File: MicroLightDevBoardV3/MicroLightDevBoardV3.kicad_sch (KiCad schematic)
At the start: 26 parts, among them J1 TYPE-C-31-M-12, J2 Conn_01x02_Socket, J3 Conn_01x03_Socket, SW1 SW_Push, U1 USBLC6-2P6, U2 STM32C071GBUx, U3 BQ25180, U4 S-85S1AB33-I6T1U

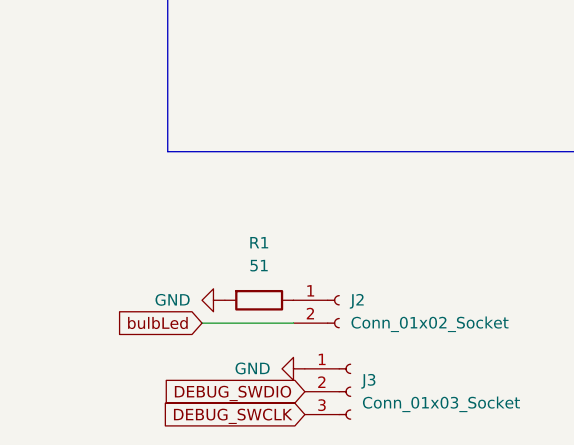
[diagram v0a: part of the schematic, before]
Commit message: adjusted debug pins to have smaller solder mask in vertical direction, changed bulb pins to both be circles and deleted 3d model, add usb 3d model
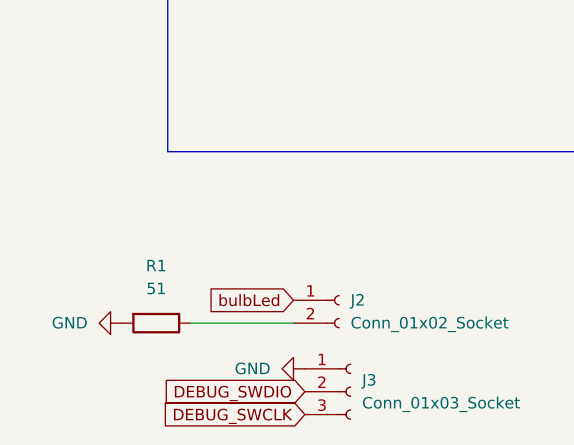
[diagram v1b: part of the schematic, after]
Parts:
- J3: footprint Connector_PinSocket_2.54mm:PinSocket_1x03_P2.54mm_Vertical -> MicroLightDevBoard:PinSocket_1x03_P2.54mm_Vertical_debug
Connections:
- net bulbLed: now also J2.1 (Pin_1); no longer J2.2 (Pin_2)
- net at R1.1: now also J2.2 (Pin_2); no longer J2.1 (Pin_1)
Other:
- moved on the sheet: R1
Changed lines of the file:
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@@
 	)
 	(no_connect
-		(at 19.05 63.5)
+		(at 41.91 55.88)
 	)
 	(no_connect
-		(at 41.91 55.88)
+		(at 19.05 63.5)
 	)
 	(no_connect
@@
 	(wire
 		(pts
-			(xy 36.83 177.8) (xy 46.99 177.8)
+			(xy 93.98 26.67) (xy 92.71 26.67)
 		)
 		(stroke
@@
 	(wire
 		(pts
-			(xy 93.98 26.67) (xy 92.71 26.67)
+			(xy 227.33 66.04) (xy 227.33 60.96)
 		)
 		(stroke
@@
 	(wire
 		(pts
-			(xy 227.33 66.04) (xy 227.33 60.96)
+			(xy 35.56 177.8) (xy 46.99 177.8)
 		)
 		(stroke
@@
 		)
 	)
-	(global_label "bulbLed"
-		(shape input)
-		(at 36.83 177.8 180)
-		(fields_autoplaced yes)
-		(effects
-			(font
-				(size 1.27 1.27)
-			)
-			(justify right)
-		)
-		(property "Intersheetrefs" "${INTERSHEET_REFS}"
-			(at 26.4669 177.8 0)
-			(effects
-				(font
-					(size 1.27 1.27)
-				)
-				(justify right)
-				(hide yes)
-			)
-		)
-	)
 	(global_label "green"
 		(shape input)
@@
 		)
 	)
+	(global_label "bulbLed"
+		(shape input)
+		(at 46.99 175.26 180)
+		(fields_autoplaced yes)
+		(effects
+			(font
+				(size 1.27 1.27)
+			)
+			(justify right)
+		)
+		(property "Intersheetrefs" "${INTERSHEET_REFS}"
+			(at 36.6269 175.26 0)
+			(effects
+				(font
+					(size 1.27 1.27)
+				)
+				(justify right)
+				(hide yes)
+			)
+		)
+	)
 	(global_label "green"
 		(shape input)
@@
 	(symbol
 		(lib_id "Device:R")
-		(at 43.18 175.26 270)
+		(at 31.75 177.8 270)
 		(unit 1)
 		(exclude_from_sim no)
@@
 		(dnp no)
 		(property "Reference" "R1"
-			(at 43.18 168.91 90)
+			(at 31.75 171.45 90)
 			(effects
 				(font
@@
 		)
 		(property "Value" "51"
-			(at 43.18 171.45 90)
+			(at 31.75 173.99 90)
 			(effects
 				(font
@@
 		)
 		(property "Footprint" "Resistor_SMD:R_0402_1005Metric"
-			(at 43.18 173.482 90)
+			(at 31.75 176.022 90)
 			(effects
 				(font
@@
 		)
 		(property "Datasheet" "~"
-			(at 43.18 175.26 0)
+			(at 31.75 177.8 0)
 			(effects
 				(font
@@
 		)
 		(property "Description" "Resistor"
-			(at 43.18 175.26 0)
+			(at 31.75 177.8 0)
 			(effects
 				(font
@@
 			)
 		)
-		(property "Footprint" "Connector_PinSocket_2.54mm:PinSocket_1x03_P2.54mm_Vertical"
+		(property "Footprint" "MicroLightDevBoard:PinSocket_1x03_P2.54mm_Vertical_debug"
 			(at 53.34 185.42 0)
 			(effects
@@
 	(symbol
 		(lib_id "power:GND")
-		(at 39.37 175.26 270)
+		(at 27.94 177.8 270)
 		(unit 1)
 		(exclude_from_sim no)
@@
 		(fields_autoplaced yes)
 		(property "Reference" "#PWR02"
-			(at 33.02 175.26 0)
+			(at 21.59 177.8 0)
 			(effects
 				(font
@@
 		)
 		(property "Value" "GND"
-			(at 35.56 175.2599 90)
+			(at 24.13 177.7999 90)
 			(effects
 				(font
@@
 		)
 		(property "Footprint" ""
-			(at 39.37 175.26 0)
+			(at 27.94 177.8 0)
 			(effects
 				(font
@@
 		)
 		(property "Datasheet" ""
-			(at 39.37 175.26 0)
+			(at 27.94 177.8 0)
 			(effects
 				(font
@@
 		)
 		(property "Description" "Power symbol creates a global label with name \"GND\" , ground"
-			(at 39.37 175.26 0)
+			(at 27.94 177.8 0)
 			(effects
 				(font

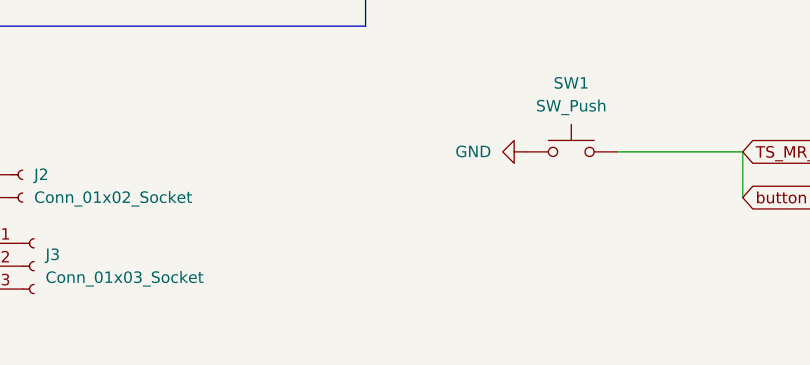
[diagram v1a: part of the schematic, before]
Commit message: change battery attachment from pad to through hole to increase durability
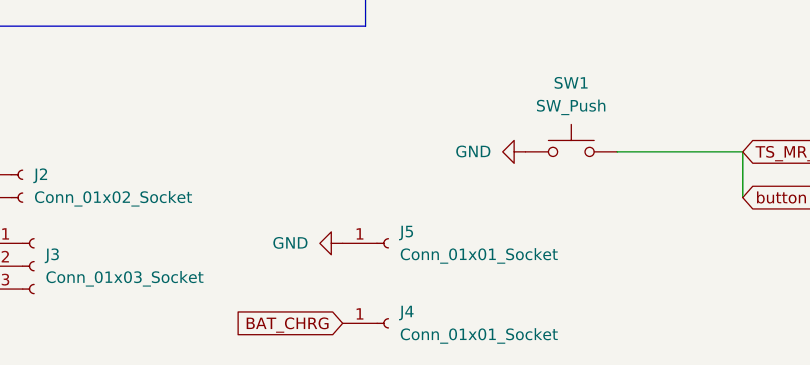
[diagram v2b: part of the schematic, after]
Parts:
- added J4, J5: Conn_01x01_Socket, MicroLightDevBoard:battery_1x01_Vertical, symbol Connector:Conn_01x01_Socket
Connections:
- net BAT_CHRG: now also J4.1 (Pin_1)
- net GND: now also J5.1 (Pin_1)
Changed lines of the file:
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@@
+	(global_label "BAT_CHRG"
+		(shape input)
+		(at 87.63 191.77 180)
+		(fields_autoplaced yes)
+		(effects
+			(font
+				(size 1.27 1.27)
+			)
+			(justify right)
+		)
+		(property "Intersheetrefs" "${INTERSHEET_REFS}"
+			(at 75.2105 191.77 0)
+			(effects
+				(font
+					(size 1.27 1.27)
+				)
+				(justify right)
+				(hide yes)
+			)
+		)
+	)
 	(global_label "BAT_CHRG"
 		(shape input)
@@
 	)
 	(symbol
+		(lib_id "Connector:Conn_01x01_Socket")
+		(at 92.71 191.77 0)
+		(unit 1)
+		(exclude_from_sim no)
+		(in_bom yes)
+		(on_board yes)
+		(dnp no)
+		(fields_autoplaced yes)
+		(property "Reference" "J4"
+			(at 93.98 190.4999 0)
+			(effects
+				(font
+					(size 1.27 1.27)
+				)
+				(justify left)
+			)
+		)
+		(property "Value" "Conn_01x01_Socket"
+			(at 93.98 193.0399 0)
+			(effects
+				(font
+					(size 1.27 1.27)
+				)
+				(justify left)
+			)
+		)
+		(property "Footprint" "MicroLightDevBoard:battery_1x01_Vertical"
+			(at 92.71 191.77 0)
+			(effects
+				(font
+					(size 1.27 1.27)
+				)
+				(hide yes)
+			)
+		)
+		(property "Datasheet" "~"
+			(at 92.71 191.77 0)
+			(effects
+				(font
+					(size 1.27 1.27)
+				)
+				(hide yes)
+			)
+		)
+		(property "Description" "Generic connector, single row, 01x01, script generated"
+			(at 92.71 191.77 0)
+			(effects
+				(font
+					(size 1.27 1.27)
+				)
+				(hide yes)
+			)
+		)
+		(pin "1"
+		)
+		(instances
+			(project ""
+				(path "/9009d70b-273c-45fe-8624-596a22a35a49"
+					(reference "J4")
+					(unit 1)
+				)
+			)
+		)
+	)
+	(symbol
 		(lib_id "MicroLightDevBoard:LED_RGBK")
 		(at 58.42 128.27 0)
@@
 	)
 	(symbol
+		(lib_id "Connector:Conn_01x01_Socket")
+		(at 92.71 182.88 0)
+		(unit 1)
+		(exclude_from_sim no)
+		(in_bom yes)
+		(on_board yes)
+		(dnp no)
+		(fields_autoplaced yes)
+		(property "Reference" "J5"
+			(at 93.98 181.6099 0)
+			(effects
+				(font
+					(size 1.27 1.27)
+				)
+				(justify left)
+			)
+		)
+		(property "Value" "Conn_01x01_Socket"
+			(at 93.98 184.1499 0)
+			(effects
+				(font
+					(size 1.27 1.27)
+				)
+				(justify left)
+			)
+		)
+		(property "Footprint" "MicroLightDevBoard:battery_1x01_Vertical"
+			(at 92.71 182.88 0)
+			(effects
+				(font
+					(size 1.27 1.27)
+				)
+				(hide yes)
+			)
+		)
+		(property "Datasheet" "~"
+			(at 92.71 182.88 0)
+			(effects
+				(font
+					(size 1.27 1.27)
+				)
+				(hide yes)
+			)
+		)
+		(property "Description" "Generic connector, single row, 01x01, script generated"
+			(at 92.71 182.88 0)
+			(effects
+				(font
+					(size 1.27 1.27)
+				)
+				(hide yes)
+			)
+		)
+		(pin "1"
+		)
+		(instances
+			(project "MicroLightDevBoardV3"
+				(path "/9009d70b-273c-45fe-8624-596a22a35a49"
+					(reference "J5")
+					(unit 1)
+				)
+			)
+		)
+	)
+	(symbol
 		(lib_id "Switch:SW_Push")
 		(at 113.03 172.72 0)
@@
 					(unit 1)
 				)
+			)
+		)
+	)
+	(symbol
+		(lib_id "power:GND")
+		(at 87.63 182.88 270)
+		(unit 1)
+		(exclude_from_sim no)
+		(in_bom yes)
+		(on_board yes)
+		(dnp no)
+		(fields_autoplaced yes)
+		(property "Reference" "#PWR024"
+			(at 81.28 182.88 0)
+			(effects
+				(font
+					(size 1.27 1.27)
+				)
+				(hide yes)
+			)
+		)
+		(property "Value" "GND"
+			(at 83.82 182.8799 90)
+			(effects
+				(font
+					(size 1.27 1.27)
+				)
+				(justify right)
+			)
+		)
+		(property "Footprint" ""
+			(at 87.63 182.88 0)
+			(effects
+				(font
+					(size 1.27 1.27)
+				)
+				(hide yes)
+			)
+		)
+		(property "Datasheet" ""
+			(at 87.63 182.88 0)
+			(effects
+				(font
+					(size 1.27 1.27)
+				)
+				(hide yes)
+			)
+		)
+		(property "Description" "Power symbol creates a global label with name \"GND\" , ground"
+			(at 87.63 182.88 0)
+			(effects
+				(font
+					(size 1.27 1.27)
+				)
+				(hide yes)
+			)
+		)
+		(pin "1"
+		)
+		(instances
+			(project "MicroLightDevBoardV3"
+				(path "/9009d70b-273c-45fe-8624-596a22a35a49"
+					(reference "#PWR024")
+					(unit 1)
+				)

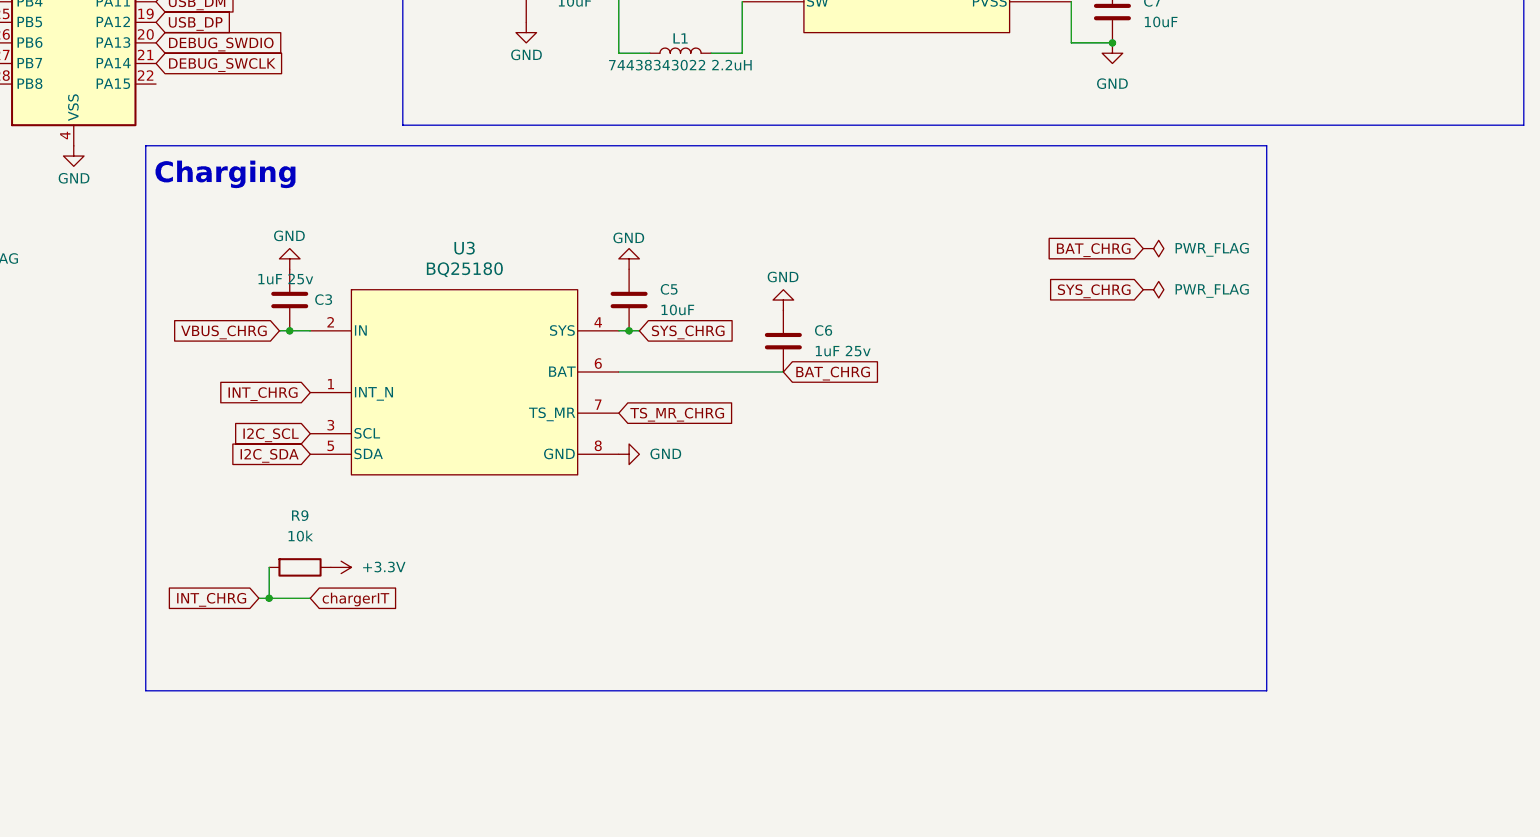
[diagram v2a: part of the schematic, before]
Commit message: use 4 layer pcb and add accelerometer ic
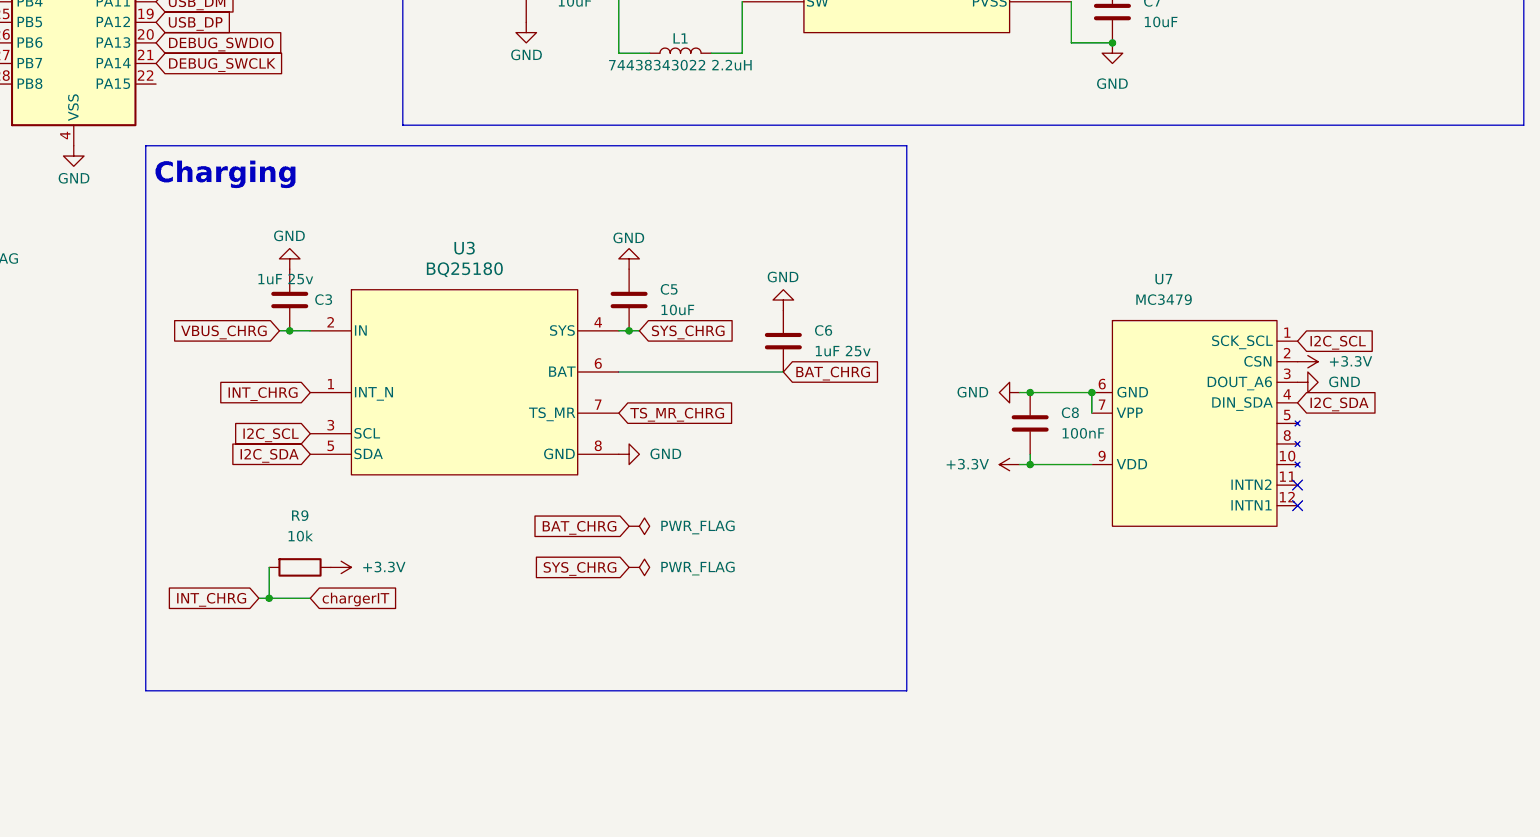
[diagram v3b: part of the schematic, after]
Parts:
- added C8: 100nF, Capacitor_SMD:C_0402_1005Metric, symbol Device:C
- added U7: MC3479, Package_LGA:LGA-12_2x2mm_P0.5mm, symbol MicroLightDevBoard:MC3479
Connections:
- net +3.3V: now also C8.2, U7.2 (CSN), U7.9 (VDD)
- net GND: now also C8.1, U7.3 (DOUT_A6), U7.6 (GND), U7.7 (VPP)
- net I2C_SCL: now also U7.1 (SCK_SCL)
- net I2C_SDA: now also U7.4 (DIN_SDA)
- no-connect marks 3 -> 5
